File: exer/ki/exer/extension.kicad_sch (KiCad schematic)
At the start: 6 parts, among them J1 Conn_01x20, J2 Conn_01x20, J3 Conn_01x34, J4 Conn_01x34, U10 74HCT574, U11 74HCT574

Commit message: Ongoing development
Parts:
- added U12, U13: 74LS125, symbol 74xx:74LS125
- added U14: 74HCT574, symbol 74xx:74HCT574
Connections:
- net U10_OE is gone; now on net GND: U10.1 (OE)
- net GND: now also J1.12 (Pin_12), U14.1 (OE), U14.10 (GND)
- net NANOIO0: now also U14.2 (D0)
- net NANOIO1: now also U14.3 (D1)
- net NANOIO2: now also U14.4 (D2)
- net NANOIO3: now also U14.5 (D3)
- net NANOIO4: now also U14.6 (D4)
- net NANOIO5: now also U14.7 (D5)
- net NANOIO6: now also U14.8 (D6)
- net NANOIO7: now also U14.9 (D7)
- net VCC: now also J2.1 (Pin_1), U12.14 (VCC), U13.14 (VCC), U14.20 (VCC)
- net TSTCLK: now reaches J1.1 (Pin_1)
- net B5_1: now reaches J1.10 (Pin_10)
- net B5_2: now reaches J1.11 (Pin_11)
- net B4_1: now reaches J1.2 (Pin_2)
- net B4_2: now reaches J1.3 (Pin_3)
- net B4_3: now reaches J1.4 (Pin_4)
- net B4_4: now reaches J1.5 (Pin_5)
- net B4_5: now reaches J1.6 (Pin_6)
- net B4_6: now reaches J1.7 (Pin_7)
- net B4_7: now reaches J1.8 (Pin_8)
- net B5_0: now reaches J1.9 (Pin_9)
- net U1_OE: now reaches U10.12 (Q7)
- net U2_OE: now reaches U10.13 (Q6)
- net U8_OE: now reaches U10.14 (Q5)
- net B10_3: now reaches U10.16 (Q3)
- net B10_2: now reaches U10.17 (Q2)
- net B10_1: now reaches U10.18 (Q1)
- net B10_0: now reaches U10.19 (Q0)
- net B11_0: now reaches U11.2 (D0)
- net B11_0: now also J2.9 (Pin_9)
- net B11_1: now reaches U11.3 (D1)
- net B11_1: now also J2.8 (Pin_8)
- net B11_2: now reaches U11.4 (D2)
- net B11_2: now also J2.7 (Pin_7)
- net B11_3: now reaches U11.5 (D3)
- net B11_3: now also J2.6 (Pin_6)
- net B11_4: now reaches U11.6 (D4)
- net B11_4: now also J2.5 (Pin_5)
- net B11_5: now reaches U11.7 (D5)
- net B11_5: now also J2.4 (Pin_4)
- net B11_6: now reaches U11.8 (D6)
- net B11_6: now also J2.3 (Pin_3)
- net B11_7: now reaches U11.9 (D7)
- net B11_7: now also J2.2 (Pin_2)
- net B3_1: now reaches J2.10 (Pin_10)
- net B3_0: now reaches J2.11 (Pin_11)
- net B5_3: now reaches J2.12 (Pin_12)
- new net: U12.7 (GND), U13.7 (GND)
- new net ENCTL0: U14.19 (Q0)
- new net ENCTL1: U14.18 (Q1)
- new net ENCTL2: U14.17 (Q2)
- new net ENCTL3: U14.16 (Q3)
- new net ENCTL4: U14.15 (Q4)
- new net ENCTL5: U14.14 (Q5)
- new net ENCTL6: U14.13 (Q6)
- new net ENCTL7: U14.12 (Q7)
- new net U14CLK: U14.11 (Cp)
- no-connect marks 0 -> 16
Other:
- moved on the sheet: J1, J2, J3, J4, U10, U11

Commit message: Ongoing development of chip exerciser
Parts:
- added NT1, NT2, NT3, NT4, NT5, NT6, NT7, NT8: NetTie_2, symbol Device:NetTie_2
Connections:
- net B11_0: now also NT8.1
- net B11_1: now also NT7.1
- net B11_2: now also NT6.1
- net B11_3: now also NT5.1
- net B11_4: now also NT4.1
- net B11_5: now also NT3.1
- net B11_6: now also NT2.1
- net B11_7: now also NT1.1
- net B4_1: now also J3.2 (Pin_2)
- net B4_2: now also J3.3 (Pin_3)
- net B4_3: now also J3.4 (Pin_4)
- net B4_4: now also J3.5 (Pin_5)
- net B4_5: now also J3.6 (Pin_6)
- net B4_6: now also J3.7 (Pin_7)
- net B4_7: now also J3.8 (Pin_8)
- net B5_0: now also J3.9 (Pin_9)
- net B5_1: now also J3.10 (Pin_10)
- net B5_2: now also J3.11 (Pin_11)
- net B5_3: now also J3.12 (Pin_12)
- net ENCTL0: now also U12.1
- net ENCTL1: now also U12.4
- net ENCTL2: now also U12.10
- net ENCTL3: now also U12.13
- net ENCTL4: now also U13.1
- net ENCTL5: now also U13.4
- net ENCTL6: now also U13.10
- net ENCTL7: now also U13.13
- net BIO6: now reaches U13.8
- net BIO6: now also NT2.2
- net B8_6: now reaches U13.9
- net BIO3: now reaches U12.11
- net BIO3: now also NT5.2
- net B8_3: now reaches U12.12
- net BIO7: now reaches U13.11
- net BIO7: now also NT1.2
- net B8_7: now reaches U13.12
- net B8_4: now reaches U13.2
- net BIO4: now reaches U13.3
- net BIO4: now also NT4.2
- net B8_5: now reaches U13.5
- net BIO5: now reaches U13.6
- net BIO5: now also NT3.2
- net B8_1: now reaches U12.5
- net BIO1: now reaches U12.6
- net BIO1: now also NT7.2
- net B1_0: now reaches J4.1 (Pin_1)
- net B2_1: now reaches J4.10 (Pin_10)
- net B2_2: now reaches J4.11 (Pin_11)
- net B2_3: now reaches J4.12 (Pin_12)
- net B2_4: now reaches J4.13 (Pin_13)
- net B2_5: now reaches J4.14 (Pin_14)
- net B2_6: now reaches J4.15 (Pin_15)
- net B2_7: now reaches J4.16 (Pin_16)
- net B1_1: now reaches J4.2 (Pin_2)
- net B1_2: now reaches J4.3 (Pin_3)
- net B1_3: now reaches J4.4 (Pin_4)
- net B1_4: now reaches J4.5 (Pin_5)
- net B1_5: now reaches J4.6 (Pin_6)
- net B1_6: now reaches J4.7 (Pin_7)
- net B1_7: now reaches J4.8 (Pin_8)
- net B2_0: now reaches J4.9 (Pin_9)
- net BIO2: now reaches U12.8
- net BIO2: now also NT6.2
- net B8_2: now reaches U12.9
- net B8_0: now reaches U12.2
- net BIO0: now reaches U12.3
- net BIO0: now also NT8.2
- net B4_0: now reaches J3.1 (Pin_1)
- net B5_4: now reaches J3.13 (Pin_13)
- net B5_5: now reaches J3.14 (Pin_14)
- net B5_6: now reaches J3.15 (Pin_15)
- net B5_7: now reaches J3.16 (Pin_16)

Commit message: Hardware design roughly complete
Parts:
- removed NT7, NT8: NetTie_2, symbol Device:NetTie_2
- added NT15, NT16: NetTie_2, symbol Device:NetTie_2
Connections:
- net B10_0: now also J4.17 (Pin_17)
- net B10_1: now also J4.18 (Pin_18)
- net B10_2: now also J4.19 (Pin_19)
- net B10_3: now also J4.20 (Pin_20)
- net B11_0: now also J3.20 (Pin_20), NT6.1
- net B11_1: now also J3.21 (Pin_21), NT5.1
- net B11_2: now also J3.22 (Pin_22), NT4.1; no longer NT6.1
- net B11_3: now also J3.23 (Pin_23), NT3.1; no longer NT5.1
- net B11_4: now also J3.24 (Pin_24), NT2.1; no longer NT4.1
- net B11_5: now also NT1.1; no longer NT3.1
- net B11_6: no longer NT2.1
- net B11_7: no longer NT1.1
- net B1_0: now also J4.16 (Pin_16); no longer J4.1 (Pin_1)
- net B1_1: now also J4.15 (Pin_15); no longer J4.2 (Pin_2)
- net B1_2: now also J4.14 (Pin_14); no longer J4.3 (Pin_3)
- net B1_3: now also J4.13 (Pin_13); no longer J4.4 (Pin_4)
- net B1_4: now also J4.12 (Pin_12); no longer J4.5 (Pin_5)
- net B1_5: now also J4.11 (Pin_11); no longer J4.6 (Pin_6)
- net B1_6: now also J4.10 (Pin_10); no longer J4.7 (Pin_7)
- net B1_7: now also J4.9 (Pin_9); no longer J4.8 (Pin_8)
- net B2_0: now also J4.8 (Pin_8); no longer J4.9 (Pin_9)
- net B2_1: now also J4.7 (Pin_7); no longer J4.10 (Pin_10)
- net B2_2: now also J4.6 (Pin_6); no longer J4.11 (Pin_11)
- net B2_3: now also J4.5 (Pin_5); no longer J4.12 (Pin_12)
- net B2_4: now also J4.4 (Pin_4); no longer J4.13 (Pin_13)
- net B2_5: now also J4.3 (Pin_3); no longer J4.14 (Pin_14)
- net B2_6: now also J4.2 (Pin_2); no longer J4.15 (Pin_15)
- net B2_7: now also J4.1 (Pin_1); no longer J4.16 (Pin_16)
- net B3_0: now also NT16.1
- net B3_1: now also J3.34 (Pin_34), NT15.1
- net B8_0: now also J3.27 (Pin_27)
- net B8_1: now also J3.26 (Pin_26)
- net B8_2: now also J3.25 (Pin_25)
- net B8_3: now also J4.25 (Pin_25)
- net B8_4: now also J4.24 (Pin_24)
- net B8_5: now also J4.23 (Pin_23)
- net B8_6: now also J4.22 (Pin_22)
- net B8_7: now also J4.21 (Pin_21)
- net BIO0: now also NT16.2
- net BIO1: now also NT15.2
- net GND: now also J3.19 (Pin_19), U12.7 (GND), U13.7 (GND)
- net TSTCLK: now also J3.17 (Pin_17)
- net VCC: now also J3.18 (Pin_18)
- net B7_0: now reaches J4.26 (Pin_26)
- net B7_1: now reaches J4.27 (Pin_27)
- net B7_2: now reaches J4.28 (Pin_28)
- net B7_3: now reaches J4.29 (Pin_29)
- net B7_4: now reaches J4.30 (Pin_30)
- net B7_5: now reaches J4.31 (Pin_31)
- net B7_6: now reaches J4.32 (Pin_32)
- net B7_7: now reaches J4.33 (Pin_33)
- net B3_7: now reaches J4.34 (Pin_34)
- net B3_7: now also J3.28 (Pin_28)
- net B3_6: now reaches J3.29 (Pin_29)
- net B3_5: now reaches J3.30 (Pin_30)
- net B3_4: now reaches J3.31 (Pin_31)
- net B3_3: now reaches J3.32 (Pin_32)
- net B3_2: now reaches J3.33 (Pin_33)
- no-connect marks 16 -> 17
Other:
- note added: ""A" PORT"
- note added: ""B" PORT"
- note added: ""F" PORT"
- moved on the sheet: U12E, U13E

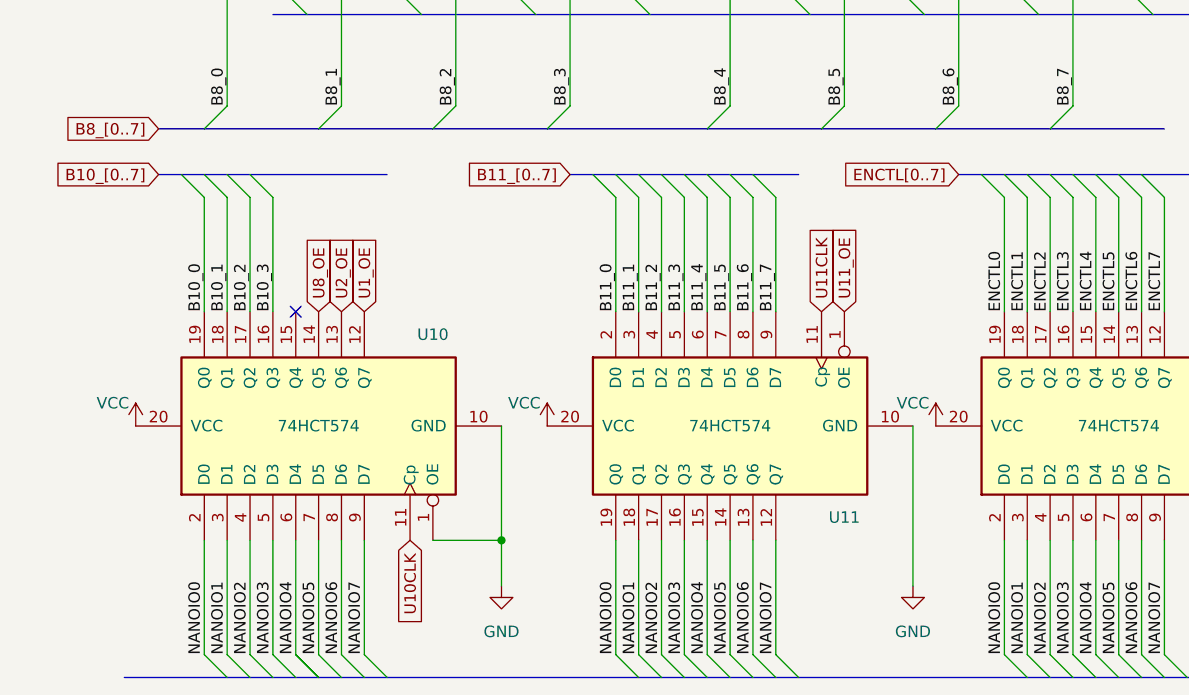
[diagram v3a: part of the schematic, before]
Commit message: Corrected labeling on U11 and U10
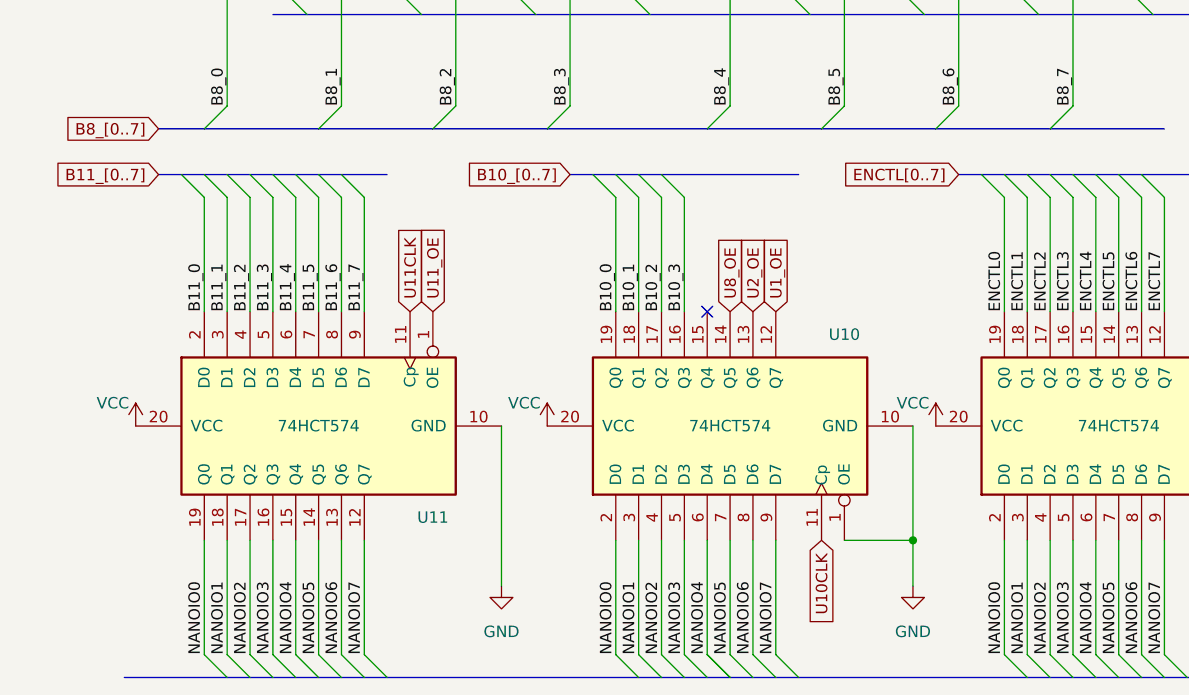
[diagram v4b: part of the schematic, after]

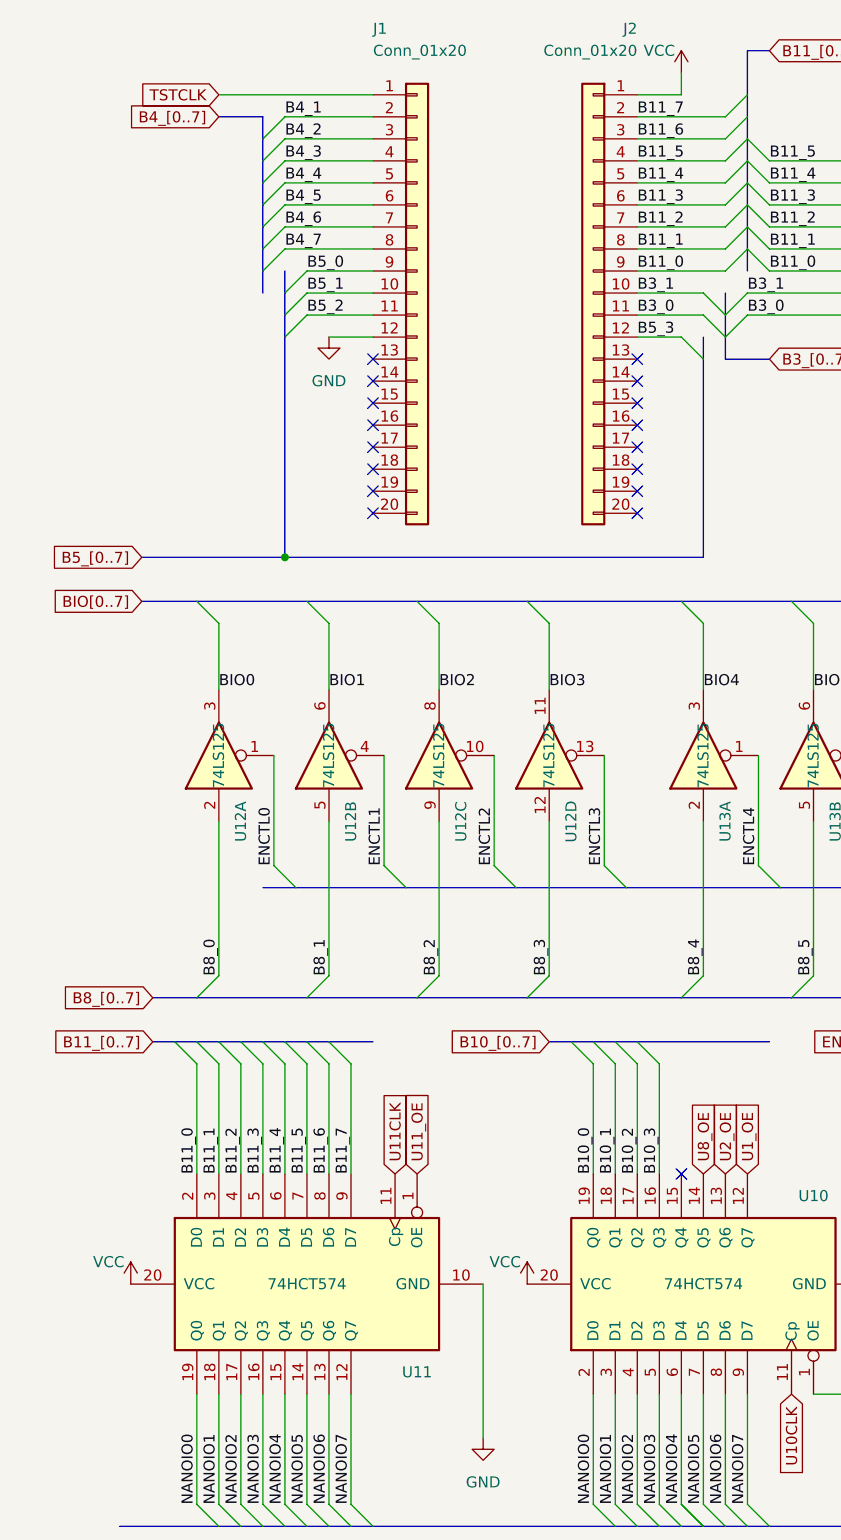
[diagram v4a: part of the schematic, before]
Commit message: Correct schematic for wiring to the 24-pin socket
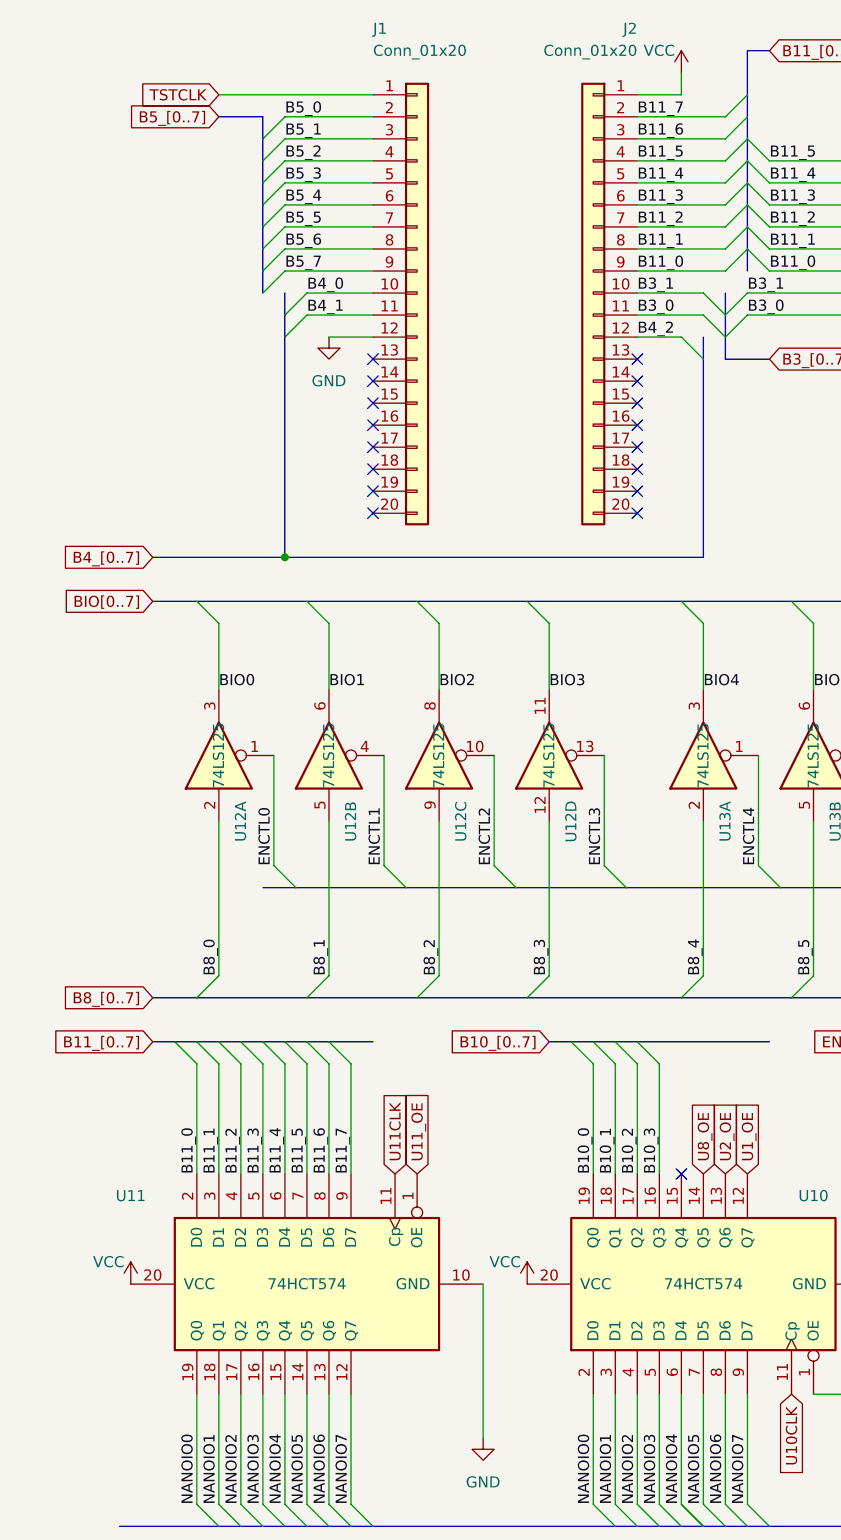
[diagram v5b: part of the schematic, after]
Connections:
- net B4_0: now also J1.10 (Pin_10)
- net B4_1: now also J1.11 (Pin_11); no longer J1.2 (Pin_2)
- net B4_2: now also J2.12 (Pin_12); no longer J1.3 (Pin_3)
- net B4_3: no longer J1.4 (Pin_4)
- net B4_4: no longer J1.5 (Pin_5)
- net B4_5: no longer J1.6 (Pin_6)
- net B4_6: no longer J1.7 (Pin_7)
- net B4_7: no longer J1.8 (Pin_8)
- net B5_0: now also J1.2 (Pin_2); no longer J1.9 (Pin_9)
- net B5_1: now also J1.3 (Pin_3); no longer J1.10 (Pin_10)
- net B5_2: now also J1.4 (Pin_4); no longer J1.11 (Pin_11)
- net B5_3: now also J1.5 (Pin_5); no longer J2.12 (Pin_12)
- net B5_4: now also J1.6 (Pin_6)
- net B5_5: now also J1.7 (Pin_7)
- net B5_6: now also J1.8 (Pin_8)
- net B5_7: now also J1.9 (Pin_9)

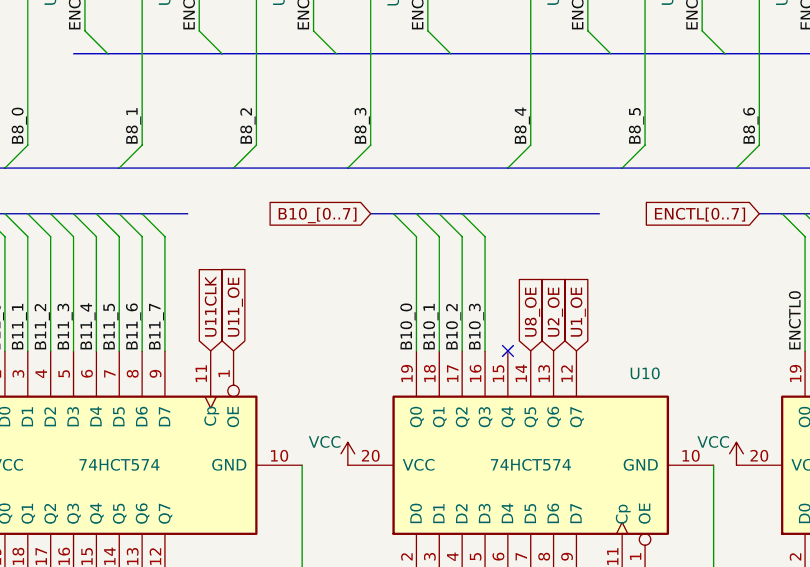
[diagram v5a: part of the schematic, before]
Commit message: Schematic corrections to OE# lines. Fix bug in firmware serial task. Implement get (g) and set (s) commands in host software cex. Changes not tested.
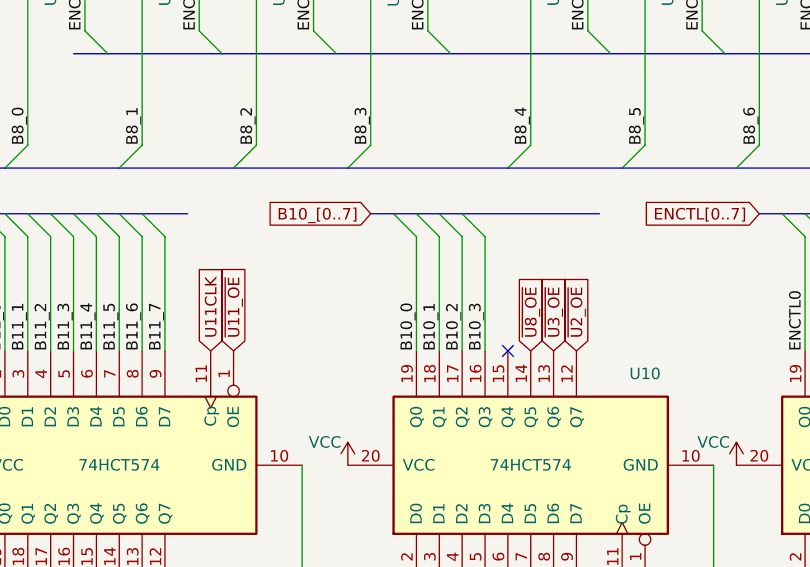
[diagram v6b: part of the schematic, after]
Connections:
- net U11_OE renamed ~{U11_OE}
- net U1_OE renamed ~{U2_OE}
- net U2_OE renamed ~{U3_OE}
- net U8_OE renamed ~{U8_OE}

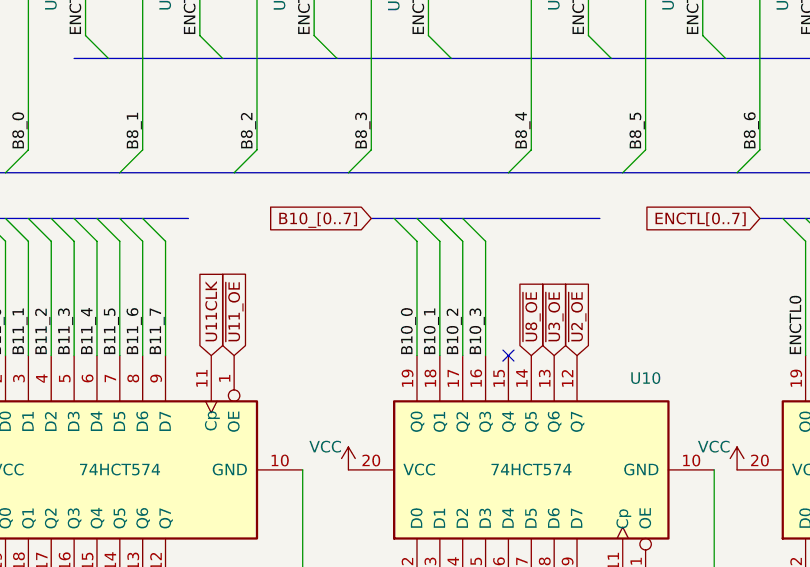
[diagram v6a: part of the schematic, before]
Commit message: Update README (still needs work). Temporarily divert main to DoVectorFile() for debugging. Much development in vector.go. Changes to U10 wiring in fact, in KiCad, in Fritzing (separate commit), and matching changes in firmware. Add test-the-tester file t.tv.
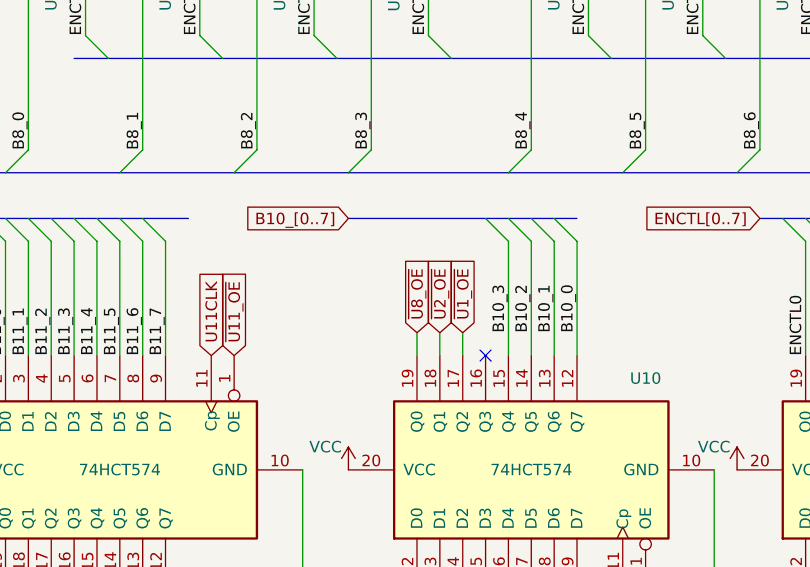
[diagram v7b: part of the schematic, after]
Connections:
- net ~{U3_OE} is gone; now on net B10_1: U10.13 (Q6)
- net B10_0: now also U10.12 (Q7); no longer U10.19 (Q0)
- net B10_1: no longer U10.18 (Q1)
- net B10_2: now also U10.14 (Q5); no longer U10.17 (Q2)
- net B10_3: now also U10.15 (Q4); no longer U10.16 (Q3)
- net ~{U2_OE}: now also U10.18 (Q1); no longer U10.12 (Q7)
- net ~{U8_OE}: now also U10.19 (Q0); no longer U10.14 (Q5)
- new net ~{U1_OE}: U10.17 (Q2)
